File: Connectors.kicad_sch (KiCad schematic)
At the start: 19 parts, among them J11 Micro_SD_Card_Det, J12 JST-PH, J13 USB_C_Receptacle_USB2.0, U10 USBLC6-2SC6

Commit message: big commit
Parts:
- added J7: EPD_Conn, grootvoet:Connector_Amphenol_10114828-xxx08LF_Vertical, symbol Connector_Generic:Conn_01x08
- added J7: LORA_Conn, grootvoet:Connector_Amphenol_10114828-xxx08LF_Vertical, symbol Connector_Generic:Conn_01x08
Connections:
- net +3V3: now also J7.1 (Pin_1), J7.1 (Pin_1)
- net GND: now also J7.2 (Pin_2), J7.2 (Pin_2)
- new net EPD_BUSY: J7.8 (Pin_8)
- new net EPD_MOSI: J7.3 (Pin_3)
- new net EPD_SCK: J7.4 (Pin_4)
- new net EPD_~{CMD}: J7.6 (Pin_6)
- new net EPD_~{RST}: J7.7 (Pin_7)
- new net EPD_~{SS}: J7.5 (Pin_5)
- new net LORA_INT: J7.8 (Pin_8)
- new net LORA_MISO: J7.3 (Pin_3)
- new net LORA_MOSI: J7.4 (Pin_4)
- new net LORA_SCK: J7.5 (Pin_5)
- new net LORA_~{RST}: J7.7 (Pin_7)
- new net LORA_~{SS}: J7.6 (Pin_6)
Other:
- note added: "EXTERNAL CONNECTORS"
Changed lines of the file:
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@@
+    (fill (type none))
+  )
+  (rectangle (start 176.022 123.698) (end 218.694 154.178)
+    (stroke (width 0) (type default))
     (fill (type none))
   )
@@
     (effects (font (size 1.27 1.27) italic) (justify left bottom))
   )
+  (text "EXTERNAL CONNECTORS" (at 176.022 123.698 0)
+    (effects (font (size 1.27 1.27) (thickness 0.254) bold) (justify left bottom))
+  )
   (text "See Application note AN10911" (at 118.11 101.6 0)
     (effects (font (size 1.27 1.27) italic) (justify left bottom))
@@
     (effects (font (size 1.27 1.27)) (justify right bottom))
   )
+  (label "EPD_SCK" (at 207.264 141.478 0) (fields_autoplaced)
+    (effects (font (size 1.27 1.27)) (justify left bottom))
+  )
+  (label "EPD_MOSI" (at 207.264 144.018 0) (fields_autoplaced)
+    (effects (font (size 1.27 1.27)) (justify left bottom))
+  )
+  (label "EPD_BUSY" (at 207.264 131.318 0) (fields_autoplaced)
+    (effects (font (size 1.27 1.27)) (justify left bottom))
+  )
+  (label "EPD_~{SS}" (at 207.264 138.938 0) (fields_autoplaced)
+    (effects (font (size 1.27 1.27)) (justify left bottom))
+  )
+  (label "EPD_~{CMD}" (at 207.264 136.398 0) (fields_autoplaced)
+    (effects (font (size 1.27 1.27)) (justify left bottom))
+  )
+  (label "LORA_~{RST}" (at 186.944 133.858 0) (fields_autoplaced)
+    (effects (font (size 1.27 1.27)) (justify left bottom))
+  )
+  (label "LORA_INT" (at 186.944 131.318 0) (fields_autoplaced)
+    (effects (font (size 1.27 1.27)) (justify left bottom))
+  )
+  (label "LORA_~{SS}" (at 186.944 136.398 0) (fields_autoplaced)
+    (effects (font (size 1.27 1.27)) (justify left bottom))
+  )
   (label "USB_CONN_D+" (at 106.68 134.62 0) (fields_autoplaced)
     (effects (font (size 1.27 1.27)) (justify left bottom))
   )
+  (label "LORA_MISO" (at 186.944 144.018 0) (fields_autoplaced)
+    (effects (font (size 1.27 1.27)) (justify left bottom))
+  )
+  (label "EPD_~{RST}" (at 207.264 133.858 0) (fields_autoplaced)
+    (effects (font (size 1.27 1.27)) (justify left bottom))
+  )
+  (label "LORA_SCK" (at 186.944 138.938 0) (fields_autoplaced)
+    (effects (font (size 1.27 1.27)) (justify left bottom))
+  )
   (label "USB_CONN_D+" (at 200.66 81.28 0) (fields_autoplaced)
+    (effects (font (size 1.27 1.27)) (justify left bottom))
+  )
+  (label "LORA_MOSI" (at 186.944 141.478 0) (fields_autoplaced)
     (effects (font (size 1.27 1.27)) (justify left bottom))
   )
@@
     )
   )
+  (symbol (lib_id "power:+3V3") (at 186.944 149.098 270) (unit 1)
+    (in_bom yes) (on_board yes) (dnp no)
+    (property "Reference" "#PWR0143" (at 183.134 149.098 0)
+      (effects (font (size 1.27 1.27)) hide)
+    )
+    (property "Value" "+3V3" (at 192.024 149.098 90)
+      (effects (font (size 1.27 1.27)))
+    )
+    (property "Footprint" "" (at 186.944 149.098 0)
+      (effects (font (size 1.27 1.27)) hide)
+    )
+    (property "Datasheet" "" (at 186.944 149.098 0)
+      (effects (font (size 1.27 1.27)) hide)
+    )
+    (pin "1")
+    (instances
+      (project "kleinvoet"
+        (path "/4185c36c-c66e-4dbd-be5d-841e551f4885/00000000-0000-0000-0000-00005edf3693"
+          (reference "#PWR0143") (unit 1)
+        )
+        (path "/4185c36c-c66e-4dbd-be5d-841e551f4885"
+          (reference "#PWR0173") (unit 1)
+        )
+        (path "/4185c36c-c66e-4dbd-be5d-841e551f4885/00000000-0000-0000-0000-00005ef53a66"
+          (reference "#PWR0143") (unit 1)
+        )
+      )
+    )
+  )
+  (symbol (lib_id "power:GND") (at 186.944 146.558 90) (unit 1)
+    (in_bom yes) (on_board yes) (dnp no)
+    (property "Reference" "#PWR0141" (at 193.294 146.558 0)
+      (effects (font (size 1.27 1.27)) hide)
+    )
+    (property "Value" "GND" (at 191.3382 146.431 90)
+      (effects (font (size 1.27 1.27)))
+    )
+    (property "Footprint" "" (at 186.944 146.558 0)
+      (effects (font (size 1.27 1.27)) hide)
+    )
+    (property "Datasheet" "" (at 186.944 146.558 0)
+      (effects (font (size 1.27 1.27)) hide)
+    )
+    (pin "1")
+    (instances
+      (project "kleinvoet"
+        (path "/4185c36c-c66e-4dbd-be5d-841e551f4885/00000000-0000-0000-0000-00005edf3693"
+          (reference "#PWR0141") (unit 1)
+        )
+        (path "/4185c36c-c66e-4dbd-be5d-841e551f4885"
+          (reference "#PWR0143") (unit 1)
+        )
+        (path "/4185c36c-c66e-4dbd-be5d-841e551f4885/00000000-0000-0000-0000-00005ef53a66"
+          (reference "#PWR0141") (unit 1)
+        )
+      )
+    )
+  )
+  (symbol (lib_id "Connector_Generic:Conn_01x08") (at 202.184 141.478 180) (unit 1)
+    (in_bom yes) (on_board yes) (dnp no) (fields_autoplaced)
+    (property "Reference" "J7" (at 202.184 126.238 0)
+      (effects (font (size 1.27 1.27)))
+    )
+    (property "Value" "EPD_Conn" (at 202.184 128.778 0)
+      (effects (font (size 1.27 1.27)))
+    )
+    (property "Footprint" "grootvoet:Connector_Amphenol_10114828-xxx08LF_Vertical" (at 202.184 141.478 0)
+      (effects (font (size 1.27 1.27)) hide)
+    )
+    (property "Datasheet" "~" (at 202.184 141.478 0)
+      (effects (font (size 1.27 1.27)) hide)
+    )
+    (pin "1")
+    (pin "2")
+    (pin "3")
+    (pin "4")
+    (pin "5")
+    (pin "6")
+    (pin "7")
+    (pin "8")
+    (instances
+      (project "kleinvoet"
+        (path "/4185c36c-c66e-4dbd-be5d-841e551f4885/00000000-0000-0000-0000-00005edf3693"
+          (reference "J7") (unit 1)
+        )
+        (path "/4185c36c-c66e-4dbd-be5d-841e551f4885"
+          (reference "J8") (unit 1)
+        )
+        (path "/4185c36c-c66e-4dbd-be5d-841e551f4885/00000000-0000-0000-0000-00005ef53a66"
+          (reference "J7") (unit 1)
+        )
+      )
+    )
+  )
   (symbol (lib_id "Device:C_Small") (at 22.86 73.66 0) (unit 1)
     (in_bom yes) (on_board yes) (dnp no)
@@
     )
   )
+  (symbol (lib_id "power:+3V3") (at 207.264 149.098 270) (unit 1)
+    (in_bom yes) (on_board yes) (dnp no)
+    (property "Reference" "#PWR0143" (at 203.454 149.098 0)
+      (effects (font (size 1.27 1.27)) hide)
+    )
+    (property "Value" "+3V3" (at 212.344 149.098 90)
+      (effects (font (size 1.27 1.27)))
+    )
+    (property "Footprint" "" (at 207.264 149.098 0)
+      (effects (font (size 1.27 1.27)) hide)
+    )
+    (property "Datasheet" "" (at 207.264 149.098 0)
+      (effects (font (size 1.27 1.27)) hide)
+    )
+    (pin "1")
+    (instances
+      (project "kleinvoet"
+        (path "/4185c36c-c66e-4dbd-be5d-841e551f4885/00000000-0000-0000-0000-00005edf3693"
+          (reference "#PWR0143") (unit 1)
+        )
+        (path "/4185c36c-c66e-4dbd-be5d-841e551f4885"
+          (reference "#PWR0175") (unit 1)
+        )
+        (path "/4185c36c-c66e-4dbd-be5d-841e551f4885/00000000-0000-0000-0000-00005ef53a66"
+          (reference "#PWR0174") (unit 1)
+        )
+      )
+    )
+  )
   (symbol (lib_id "power:GND") (at 43.18 80.01 0) (unit 1)
     (in_bom yes) (on_board yes) (dnp no)
@@
         )
       )
+    )
+  )
+  (symbol (lib_id "Connector_Generic:Conn_01x08") (at 181.864 141.478 180) (unit 1)
+    (in_bom yes) (on_board yes) (dnp no) (fields_autoplaced)
+    (property "Reference" "J7" (at 181.864 126.238 0)
+      (effects (font (size 1.27 1.27)))
+    )
+    (property "Value" "LORA_Conn" (at 181.864 128.778 0)
+      (effects (font (size 1.27 1.27)))
+    )
+    (property "Footprint" "grootvoet:Connector_Amphenol_10114828-xxx08LF_Vertical" (at 181.864 141.478 0)
+      (effects (font (size 1.27 1.27)) hide)
+    )
+    (property "Datasheet" "~" (at 181.864 141.478 0)
+      (effects (font (size 1.27 1.27)) hide)
+    )
+    (pin "1")
+    (pin "2")
+    (pin "3")
+    (pin "4")
+    (pin "5")
+    (pin "6")
+    (pin "7")
+    (pin "8")
+    (instances
+      (project "kleinvoet"
+        (path "/4185c36c-c66e-4dbd-be5d-841e551f4885/00000000-0000-0000-0000-00005edf3693"
+          (reference "J7") (unit 1)
+        )
+        (path "/4185c36c-c66e-4dbd-be5d-841e551f4885"
+          (reference "J7") (unit 1)
+        )
+        (path "/4185c36c-c66e-4dbd-be5d-841e551f4885/00000000-0000-0000-0000-00005ef53a66"
+          (reference "J5") (unit 1)
+        )
+      )
+    )
+  )
+  (symbol (lib_id "power:GND") (at 207.264 146.558 90) (unit 1)
+    (in_bom yes) (on_board yes) (dnp no)
+    (property "Reference" "#PWR0141" (at 213.614 146.558 0)
+      (effects (font (size 1.27 1.27)) hide)
+    )
+    (property "Value" "GND" (at 211.6582 146.431 90)
+      (effects (font (size 1.27 1.27)))
+    )
+    (property "Footprint" "" (at 207.264 146.558 0)
+      (effects (font (size 1.27 1.27)) hide)
+    )
+    (property "Datasheet" "" (at 207.264 146.558 0)
+      (effects (font (size 1.27 1.27)) hide)
+    )
+    (pin "1")
+    (instances
+      (project "kleinvoet"
+        (path "/4185c36c-c66e-4dbd-be5d-841e551f4885/00000000-0000-0000-0000-00005edf3693"
+          (reference "#PWR0141") (unit 1)
+        )
+        (path "/4185c36c-c66e-4dbd-be5d-841e551f4885"
+          (reference "#PWR0174") (unit 1)
+        )
+        (path "/4185c36c-c66e-4dbd-be5d-841e551f4885/00000000-0000-0000-0000-00005ef53a66"
+          (reference "#PWR0173") (unit 1)
+        )
+      )

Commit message: Big commit for the day
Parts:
- added J1: Conn_ST_STDC14, grootvoet:Tag-Connect_TC2050-IDC-STDC14-FP_2x05_P1.27mm_Vertical, symbol Connector:Conn_ST_STDC14
- added J10: VCP_CONN, symbol Connector_Generic:Conn_01x02
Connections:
- net +3V3: now also J1.3 (T_VCC)
- net GND: now also J1.11 (GNDDetect), J1.5 (GND), J1.7 (GND)
- new net SWD_CLK: J1.6 (JCLK/SWCLK)
- new net SWD_DIO: J1.4 (JTMS/SWDIO)
- new net SWD_O: J1.8 (JTDO/SWO)
- new net SWD_~{RST}: J1.12 (~{RST})
- new net VCP_RX: J1.13 (VCP_RX), J10.2 (Pin_2)
- new net VCP_TX: J1.14 (VCP_TX), J10.1 (Pin_1)
- no-connect marks 2 -> 6
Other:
- note added: "Debug Connector"
- note added: "See Manual UM2502"

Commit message: (sch) change debug footprint
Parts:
- J1: value Conn_ST_STDC14 -> DNP; footprint grootvoet:Tag-Connect_TC2050-IDC-STDC14-FP_2x05_P1.27mm_Vertical -> Connector:Tag-Connect_TC2070-IDC-FP_2x07_P1.27mm_Vertical
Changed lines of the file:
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@@
       (effects (font (size 1.27 1.27)) (justify right))
     )
-    (property "Value" "Conn_ST_STDC14" (at 32.385 153.67 0)
+    (property "Value" "DNP" (at 32.385 153.67 0)
       (effects (font (size 1.27 1.27)) (justify right))
     )
-    (property "Footprint" "grootvoet:Tag-Connect_TC2050-IDC-STDC14-FP_2x05_P1.27mm_Vertical" (at 41.275 196.85 0)
+    (property "Footprint" "Connector:Tag-Connect_TC2070-IDC-FP_2x07_P1.27mm_Vertical" (at 41.275 196.85 0)
       (effects (font (size 1.27 1.27)) hide)
     )

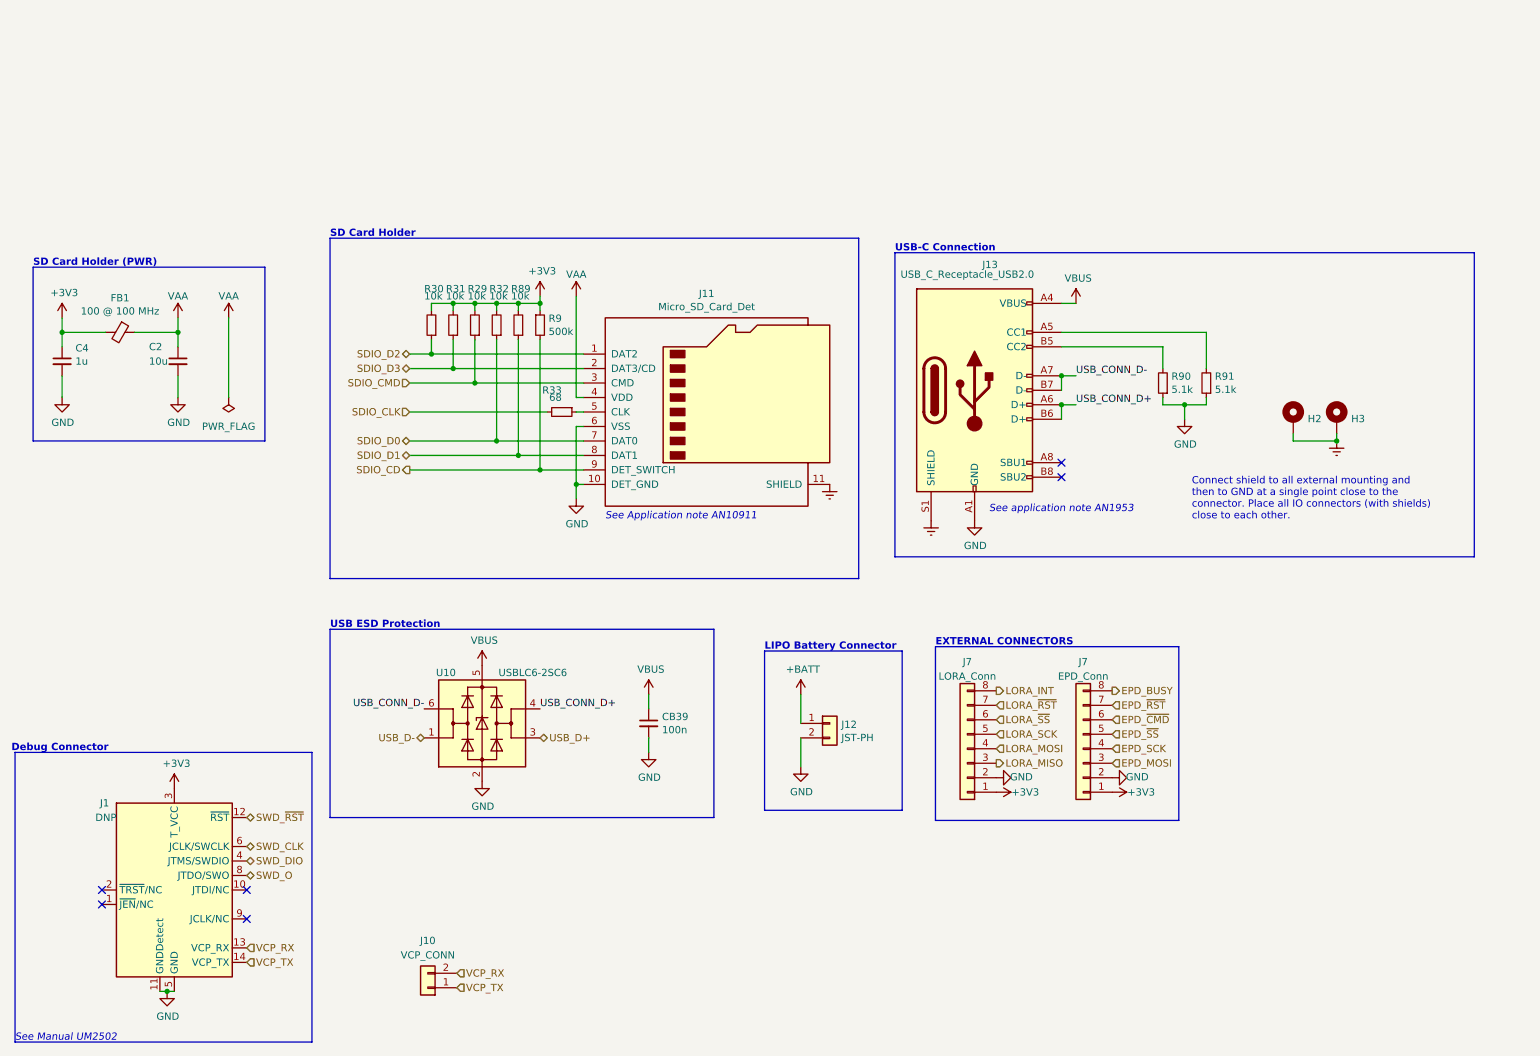
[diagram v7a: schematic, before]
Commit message: (sch) add serial pin interface
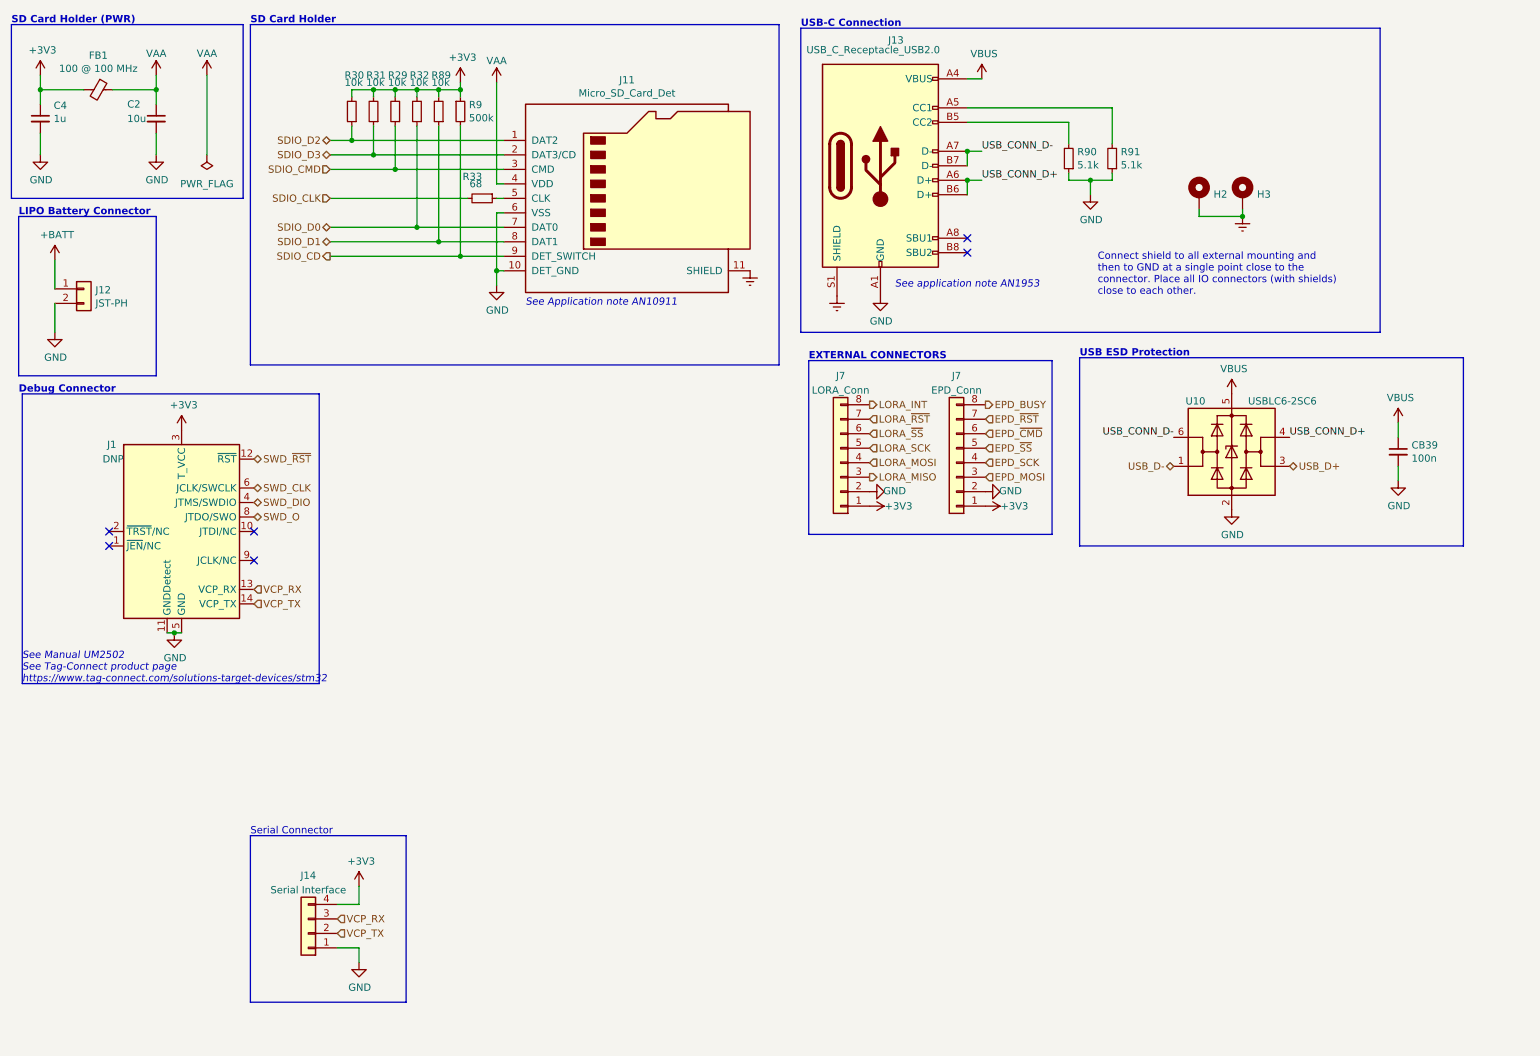
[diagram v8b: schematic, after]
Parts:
- removed J10: VCP_CONN, symbol Connector_Generic:Conn_01x02
- added J14: Serial Interface, Connector_PinHeader_1.27mm:PinHeader_1x04_P1.27mm_Vertical, symbol Connector_Generic:Conn_01x04
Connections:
- net +3V3: now also J14.4 (Pin_4)
- net GND: now also J14.1 (Pin_1)
- net VCP_RX: now also J14.3 (Pin_3)
- net VCP_TX: now also J14.2 (Pin_2)
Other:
- note added: "See Manual UM2502 See Tag-Connect product page https://www.tag-connect.com/solutions-target-devices/stm32"
- note added: "Serial Connector"
- note removed: "See Manual UM2502"
- moved on the sheet: C2, C4, CB39, FB1, H2, H3, J1, J11, J12, J13, J7, R29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
